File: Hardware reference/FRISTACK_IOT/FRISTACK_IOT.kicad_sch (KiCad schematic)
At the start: 57 parts, among them J1 MEM2075-00-140-01-A, J2 Conn_01x02_Pin, J3 Conn_01x13_Socket, J4 Conn_01x13_Socket, U1 TPS62840DLCR, U2 ESP32-C6-MINI-1-H4, U3 SN65HVD232, Y1 32.768 kHz

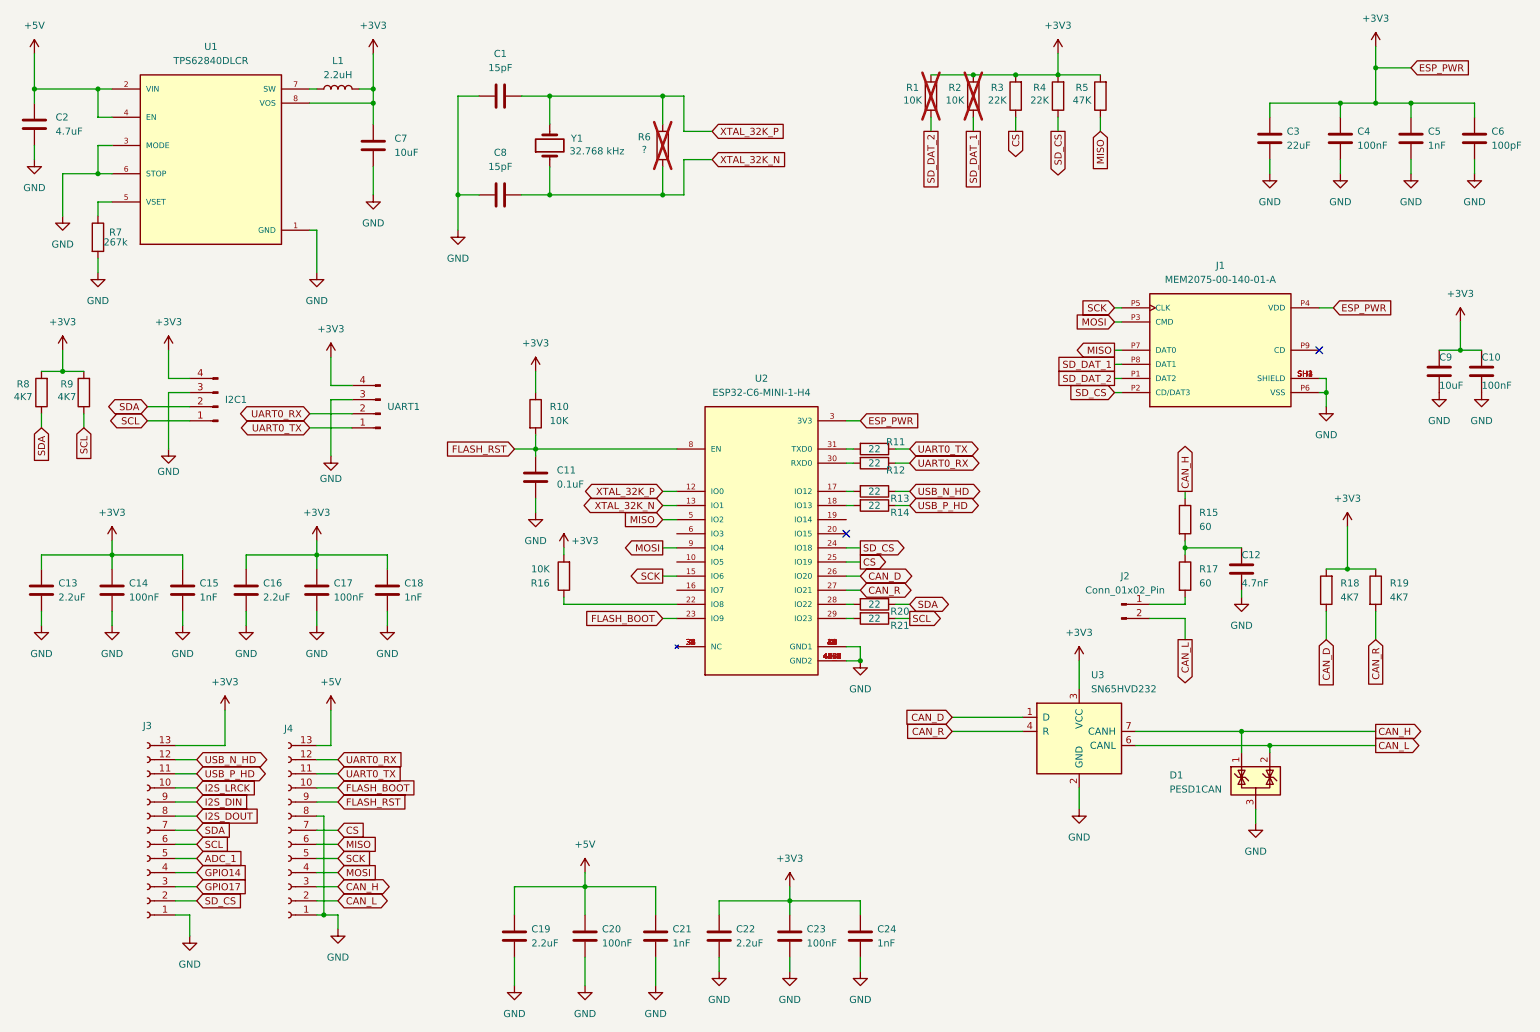
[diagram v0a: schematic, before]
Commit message: review and new BATTERY board
IOT - changed twai termination from header to switch option, new holes , added power planes
SENSOR NODE - new holes and back silk text
CORE - vertical twai termination header changed to horizontal
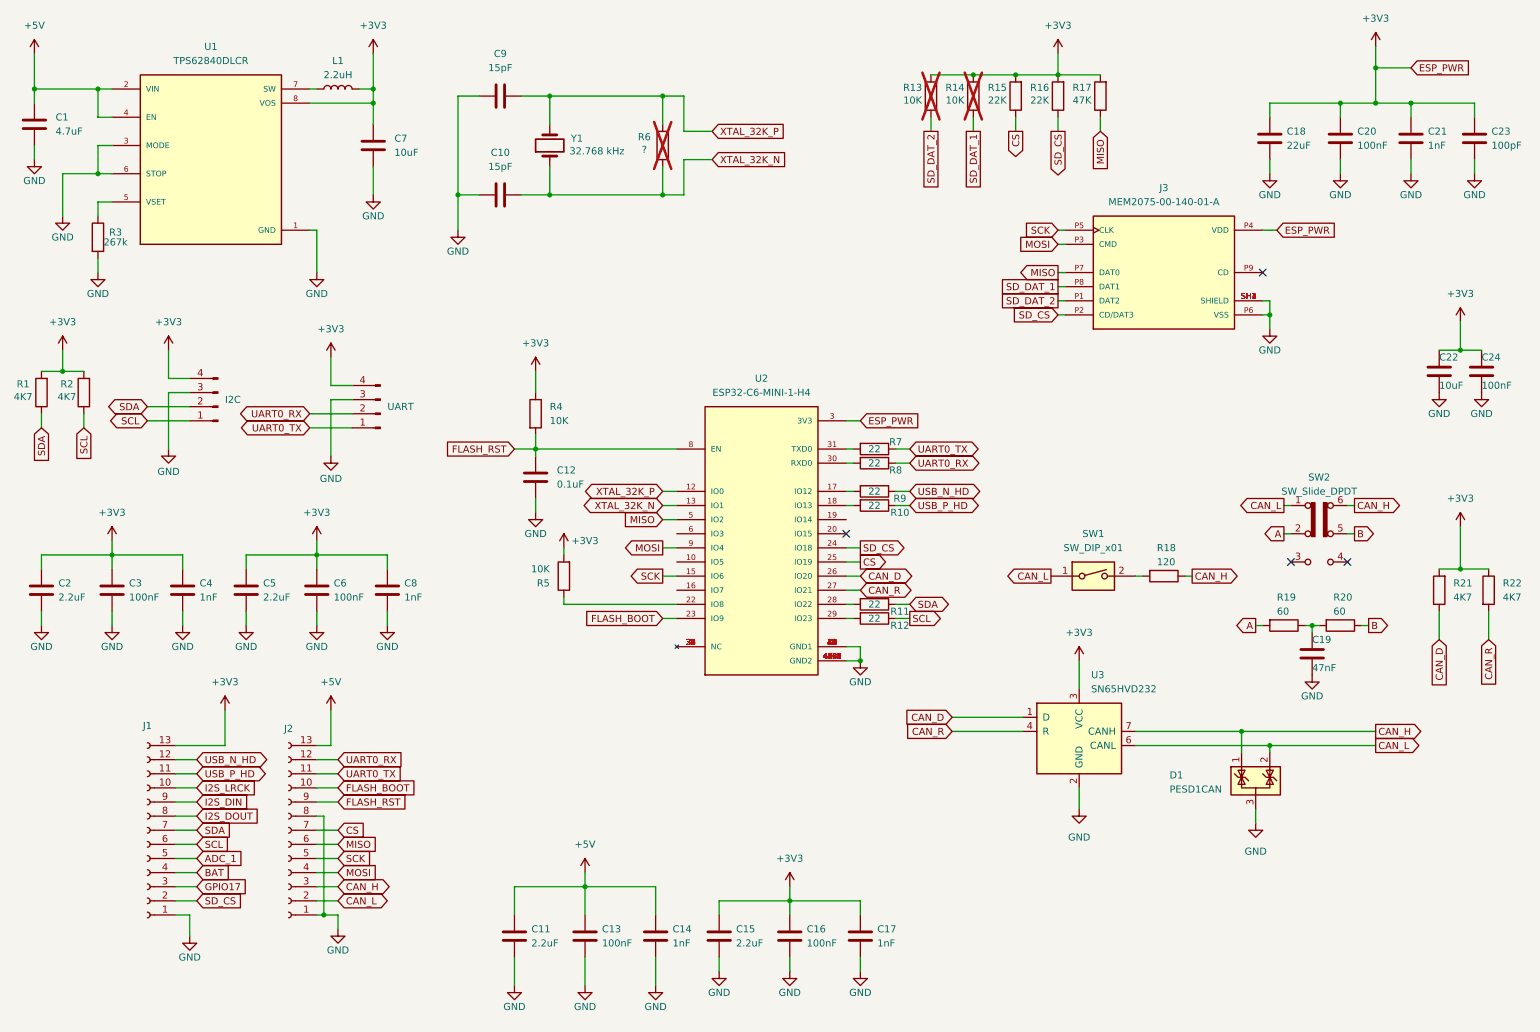
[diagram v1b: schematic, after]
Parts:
- removed C12: 4.7nF, Capacitor_SMD:C_0603_1608Metric, symbol Device:C
- removed J2: Conn_01x02_Pin, Connector_PinHeader_2.54mm:PinHeader_1x02_P2.54mm_Vertical, symbol Connector:Conn_01x02_Pin
- removed R15, R17: 60, Resistor_SMD:R_0603_1608Metric, symbol Device:R
- added C19: 47nF, Capacitor_SMD:C_0603_1608Metric, symbol Device:C
- added R18: 120, Resistor_SMD:R_0603_1608Metric, symbol Device:R
- added R19, R20: 60, Resistor_SMD:R_0603_1608Metric, symbol Device:R
- added SW1: SW_DIP_x01, Button_Switch_THT:SW_DIP_SPSTx01_Slide_6.7x4.1mm_W7.62mm_P2.54mm_LowProfile, symbol Switch:SW_DIP_x01
- added SW2: SW_Slide_DPDT, Button_Switch_SMD:SW_DPDT_CK_JS202011JCQN, symbol Switch:SW_Slide_DPDT
- renumbered C2 to C1, C8 to C10, C19 to C11, C11 to C12, C20 to C13, C21 to C14, C22 to C15, C23 to C16, C24 to C17, C3 to C18, C13 to C2, C4 to C20, C5 to C21, C9 to C22, C6 to C23, C10 to C24, C14 to C3, C15 to C4, C16 to C5, C17 to C6, C18 to C8, C1 to C9, I2C1 to I2C, J3 to J1, J4 to J2, J1 to J3, R8 to R1, R14 to R10, R20 to R11, R21 to R12, R1 to R13, R2 to R14, R3 to R15, R4 to R16, R5 to R17, R9 to R2, R18 to R21, R19 to R22, R7 to R3, R10 to R4, R16 to R5, R11 to R7, R12 to R8, R13 to R9, UART1 to UART
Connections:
- net CAN_H: now also R18.1, SW2.6 (C)
- net CAN_L: now also SW1.1, SW2.1 (A)
- net GND: now also C19.2
- net GPIO14 renamed BAT
- new net: C19.1, R19.1, R20.2
- new net: R18.2, SW1.2
- new net A: R19.2, SW2.2 (B)
- new net B: R20.1, SW2.5 (B)
- no-connect marks 2 -> 4
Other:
- moved on the sheet: J3, R21, R22
